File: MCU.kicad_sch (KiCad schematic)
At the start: 23 parts, among them J2 USB_B_Micro, U1 ECS-TXO-2016, U4 STM32L476RGTx, U5 USBLC6-2SC6, Y1 32768Hz

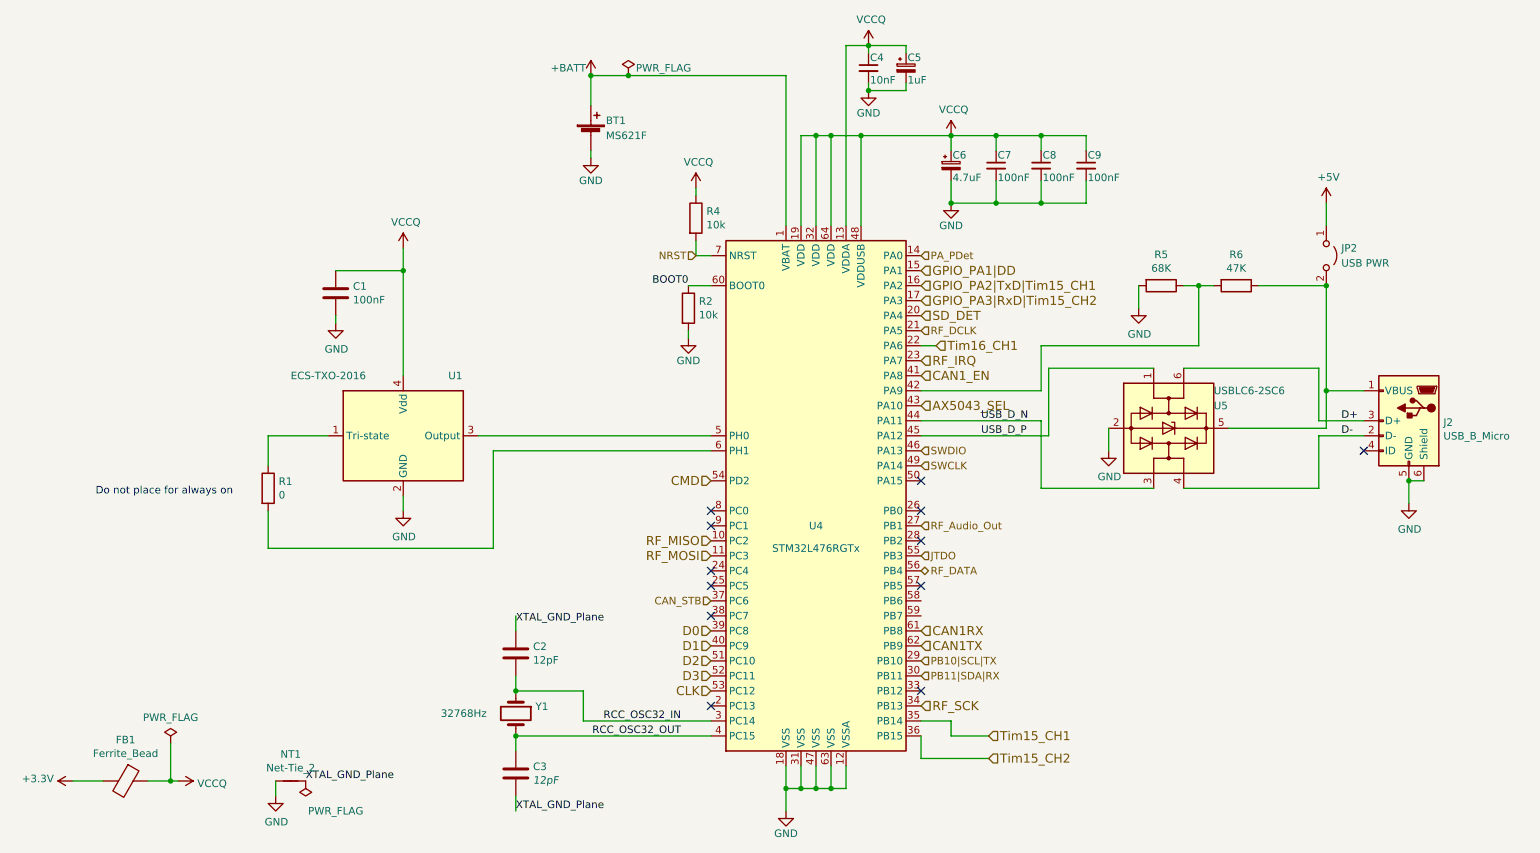
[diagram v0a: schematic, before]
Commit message: Clean-up schematic
Closes #4
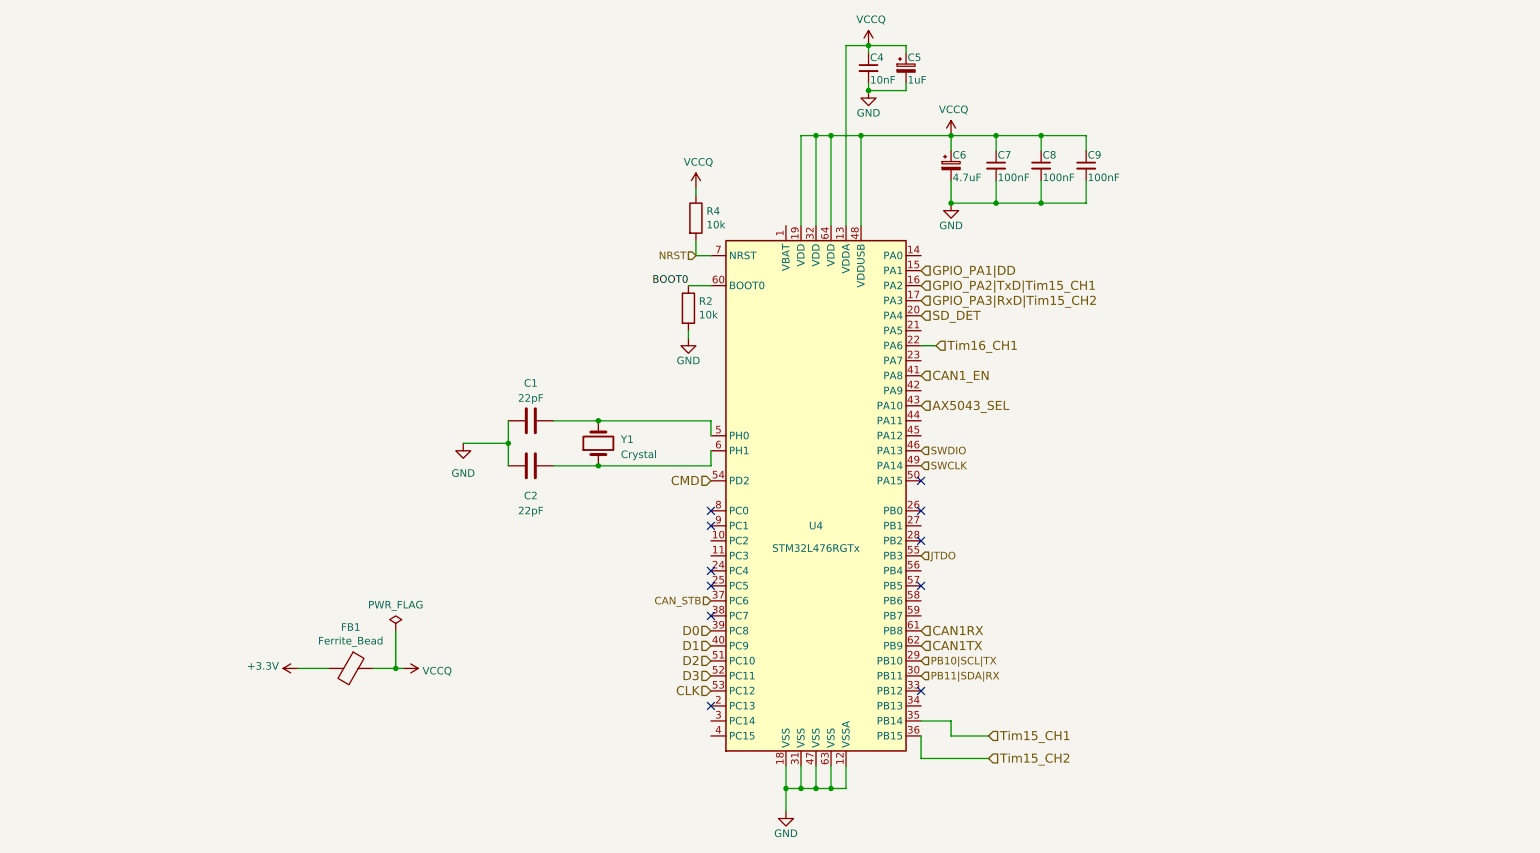
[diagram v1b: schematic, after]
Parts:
- removed BT1: MS621F, Battery:BatteryHolder_Seiko_MS621F, symbol Device:Battery_Cell
- removed C3: 12pF, Capacitor_SMD:C_0603_1608Metric, symbol Device:C
- removed J2: USB_B_Micro, Connector_USB:USB_Micro-B_Molex_47346-0001, symbol Connector:USB_B_Micro
- removed JP2: USB PWR, Jumper:SolderJumper-2_P1.3mm_Open_Pad1.0x1.5mm, symbol Jumper:Jumper_2_Open
- removed NT1: Net-Tie_2, NetTie:NetTie-2_SMD_Pad0.5mm, symbol Device:NetTie_2
- removed R1: 0, Resistor_SMD:R_0603_1608Metric_Pad1.05x0.95mm_HandSolder, symbol Device:R
- removed R5: 68K, Resistor_SMD:R_0603_1608Metric_Pad1.05x0.95mm_HandSolder, symbol Device:R
- removed R6: 47K, Resistor_SMD:R_0603_1608Metric_Pad1.05x0.95mm_HandSolder, symbol Device:R
- removed U1: ECS-TXO-2016, lsf-kicad-lib:Oscillator_SMD_ECS_TXO-2016-xx-xxx-4Pin_2x1.6mm, symbol lsf-kicad:ECS-TXO-2016
- removed U5: USBLC6-2SC6, Package_TO_SOT_SMD:SOT-23-6, symbol Power_Protection:USBLC6-2SC6
- C1: value 100nF -> 22pF; footprint Capacitor_SMD:C_0603_1608Metric -> (none); Part Number C0603C104K9RACTU -> (none)
- C2: value 12pF -> 22pF; footprint Capacitor_SMD:C_0603_1608Metric -> (none); Part Number CBR06C120FAGAC -> (none)
- Y1: value 32768Hz -> Crystal; footprint Crystal:Crystal_SMD_3215-2Pin_3.2x1.5mm -> Crystal:Crystal_SMD_HC49-SD; MPN (none) -> ECS-80-18-5PX-CKM-TR; Part Number ABS07-32.768KHZ-7-T -> (none)
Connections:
- net XTAL_GND_Plane is gone; now on net GND: C2.1
- net GND: now also C1.1; no longer C1.2
- net VCCQ: no longer C1.1
- net at U4.5 (PH0): now also C1.2, Y1.2
- net at U4.6 (PH1): now also C2.2, Y1.1
- net +BATT: no longer names the net of U4.1 (VBAT)
- net PA_PDet: no longer names the net of U4.14 (PA0)
- removed net RCC_OSC32_IN: C2.2, U4.3 (PC14), Y1.1
- net RCC_OSC32_OUT: no longer names the net of U4.4 (PC15)
- net RCC_OSC32_OUT: no longer Y1.2
- net RF_Audio_Out: no longer names the net of U4.27 (PB1)
- net RF_DATA: no longer names the net of U4.56 (PB4)
- net RF_DCLK: no longer names the net of U4.21 (PA5)
- net RF_IRQ: no longer names the net of U4.23 (PA7)
- net RF_MISO: no longer names the net of U4.10 (PC2)
- net RF_MOSI: no longer names the net of U4.11 (PC3)
- net RF_SCK: no longer names the net of U4.34 (PB13)
- net USB_D_N: no longer names the net of U4.44 (PA11)
- net USB_D_P: no longer names the net of U4.45 (PA12)
- no-connect marks 12 -> 11
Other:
- note removed: "Do not place for always on"
- moved on the sheet: FB1

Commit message: Add connections between existing sheets
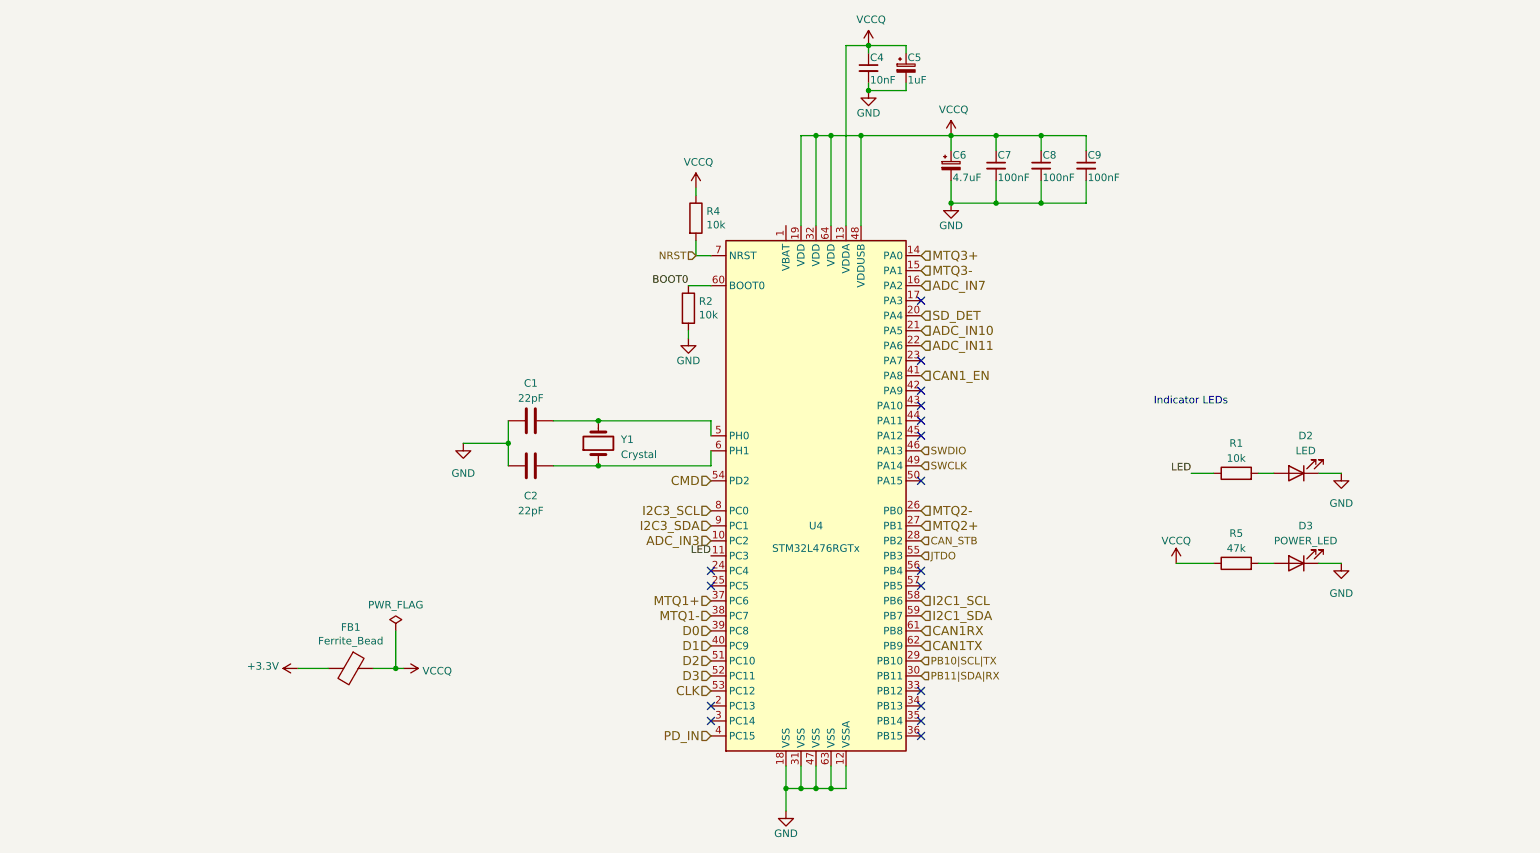
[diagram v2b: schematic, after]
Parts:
- added D2: LED, LED_SMD:LED_0603_1608Metric, symbol Device:LED
- added D3: POWER_LED, LED_SMD:LED_0603_1608Metric, symbol Device:LED
- added R1: 10k, Resistor_SMD:R_0603_1608Metric, symbol Device:R
- added R5: 47k, Resistor_SMD:R_0603_1608Metric, symbol Device:R
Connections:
- net CAN_STB: now also U4.28 (PB2); no longer U4.37 (PC6)
- net GND: now also D2.1 (K), D3.1 (K)
- net VCCQ: now also R5.1
- net ADC_IN3: now reaches U4.10 (PC2)
- net LED: now reaches U4.11 (PC3)
- net LED: now also R1.1
- net MTQ3+: now reaches U4.14 (PA0)
- net ADC_IN10: now reaches U4.21 (PA5)
- net MTQ2-: now reaches U4.26 (PB0)
- net MTQ2+: now reaches U4.27 (PB1)
- net MTQ1-: now reaches U4.38 (PC7)
- net PD_IN: now reaches U4.4 (PC15)
- net I2C1_SCL: now reaches U4.58 (PB6)
- net I2C1_SDA: now reaches U4.59 (PB7)
- net I2C3_SCL: now reaches U4.8 (PC0)
- net I2C3_SDA: now reaches U4.9 (PC1)
- net AX5043_SEL: no longer names the net of U4.43 (PA10)
- net GPIO_PA1|DD renamed MTQ3-
- net GPIO_PA2|TxD|Tim15_CH1 renamed ADC_IN7
- net GPIO_PA3|RxD|Tim15_CH2: no longer names the net of U4.17 (PA3)
- net Tim15_CH1: no longer names the net of U4.35 (PB14)
- net Tim15_CH2: no longer names the net of U4.36 (PB15)
- net Tim16_CH1 renamed ADC_IN11
- new net: D3.2 (A), R5.2
- new net: D2.2 (A), R1.2
- new net MTQ1+: U4.37 (PC6)
- no-connect marks 11 -> 17
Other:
- note added: "Indicator LEDs"

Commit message: Reannotate schematic
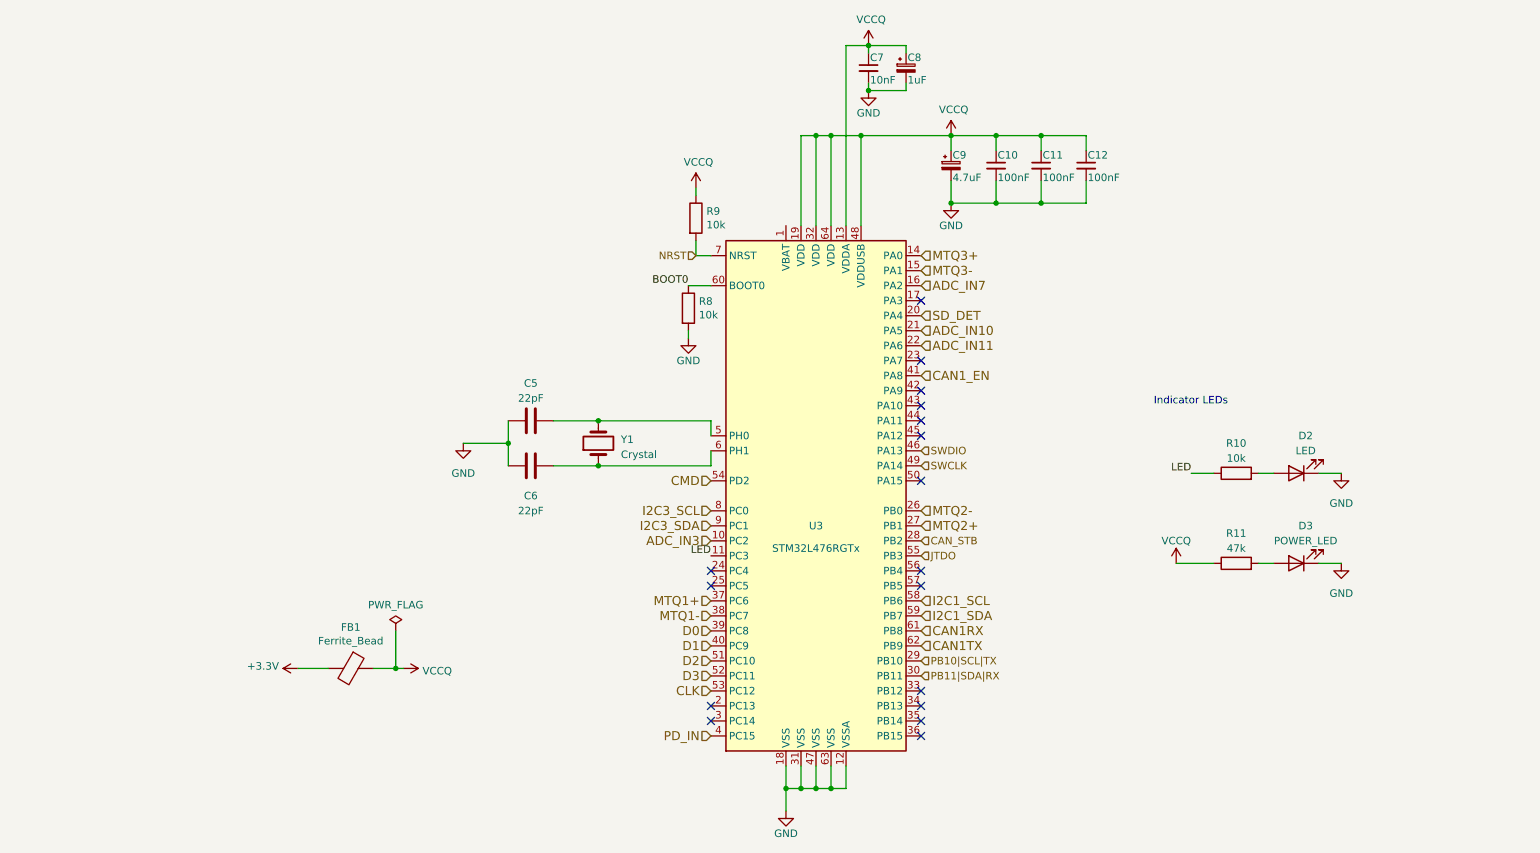
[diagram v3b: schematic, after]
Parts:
- renumbered C7 to C10, C8 to C11, C9 to C12, C1 to C5, C2 to C6, C4 to C7, C5 to C8, C6 to C9, R1 to R10, R5 to R11, R2 to R8, R4 to R9, U4 to U3
